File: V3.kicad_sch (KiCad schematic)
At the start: 30 parts, among them J1 USB_B, J2 Conn_01x02, J4 MAX9814, J5 OLED, J6 Heartbeat, Q1 AO3401A, U1 AP9101CK-CMTRG1, U2 AMS1117-3.3, U3 ESP32-S2-WROVER, U4 MMA8652FCR1

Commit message: Finalise schematic and start routing
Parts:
- removed TP2: TP_Battery+, TestPoint:TestPoint_Pad_D1.0mm, symbol Connector:TestPoint
- removed TP4: TP_Battery-, TestPoint:TestPoint_Pad_D1.0mm, symbol Connector:TestPoint
- removed U2: AMS1117-3.3, Package_TO_SOT_SMD:SOT-223-3_TabPin2, symbol Regulator_Linear:AMS1117-3.3
- added R8: 45K, Resistor_SMD:R_1206_3216Metric, symbol Device:R_Small
- added U2: XC6222B331MR-G, Package_TO_SOT_SMD:SOT-23-5, symbol Regulator_Linear:XC6220B331MR
- C1, C2: value 100uF -> 1uF; footprint Capacitor_SMD:C_1812_4532Metric -> Capacitor_SMD:C_1206_3216Metric
- J3: value (none) -> 47219-2001; footprint (none) -> 3rdparty:MOLEX_47219-2001
- Q3: value (none) -> BSD840NH6327XTSA1; footprint (none) -> Package_TO_SOT_SMD:SOT-363_SC-70-6
- renumbered TP5 to 3v3
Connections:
- net +3V3: now also R8.2, U2.5 (VOUT)
- net GND: now also U2.2 (GND)
- net VCC: now also U2.1 (VIN), U2.3 (CE)
- net at U3.21 (IO18): now also R8.1
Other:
- note added: "I2C Addr: 0x1D"
- note added: "Simulation: https://tinyurl.com/y7ddr9ho"
- moved on the sheet: 3v3, C2, C3, R5, TP6

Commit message: Finish routing and export gerbers
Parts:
- added R10, R9: 4.7K, Resistor_SMD:R_1206_3216Metric, symbol Device:R_Small
- added U5: USBLC6-2SC6, Package_TO_SOT_SMD:SOT-23-6, symbol Power_Protection:USBLC6-2SC6
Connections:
- net +3V3: now also R10.2, R9.2
- net GND: now also U5.2 (GND)
- net SCL: now also R10.1
- net SDA: now also R9.1
- net USB_D+: now also U5.1 (I/O1); no longer J1.3 (D+)
- net USB_D-: now also U5.3 (I/O2); no longer J1.2 (D-)
- net VBUS: now also U5.5 (VBUS)
- new net USB_CONN_D+: J1.3 (D+), U5.6 (I/O1)
- new net USB_CONN_D-: J1.2 (D-), U5.4 (I/O2)
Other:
- moved on the sheet: R4, R6, R7, U3

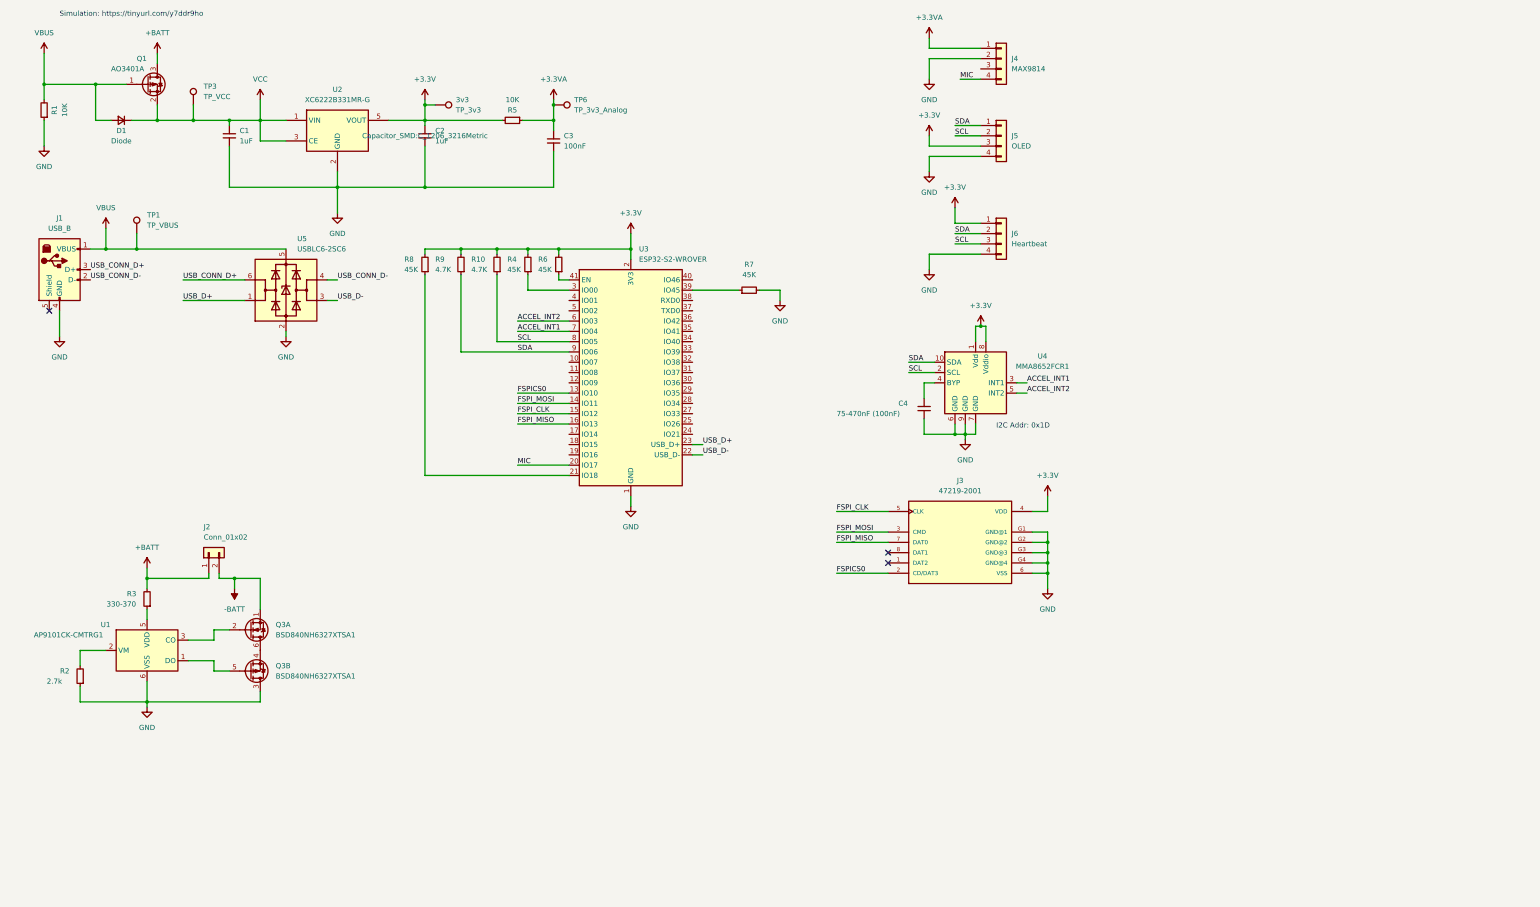
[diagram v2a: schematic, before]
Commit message: Add 3d models, pcb & schematic touch up, graphics, update gerbers and add step file
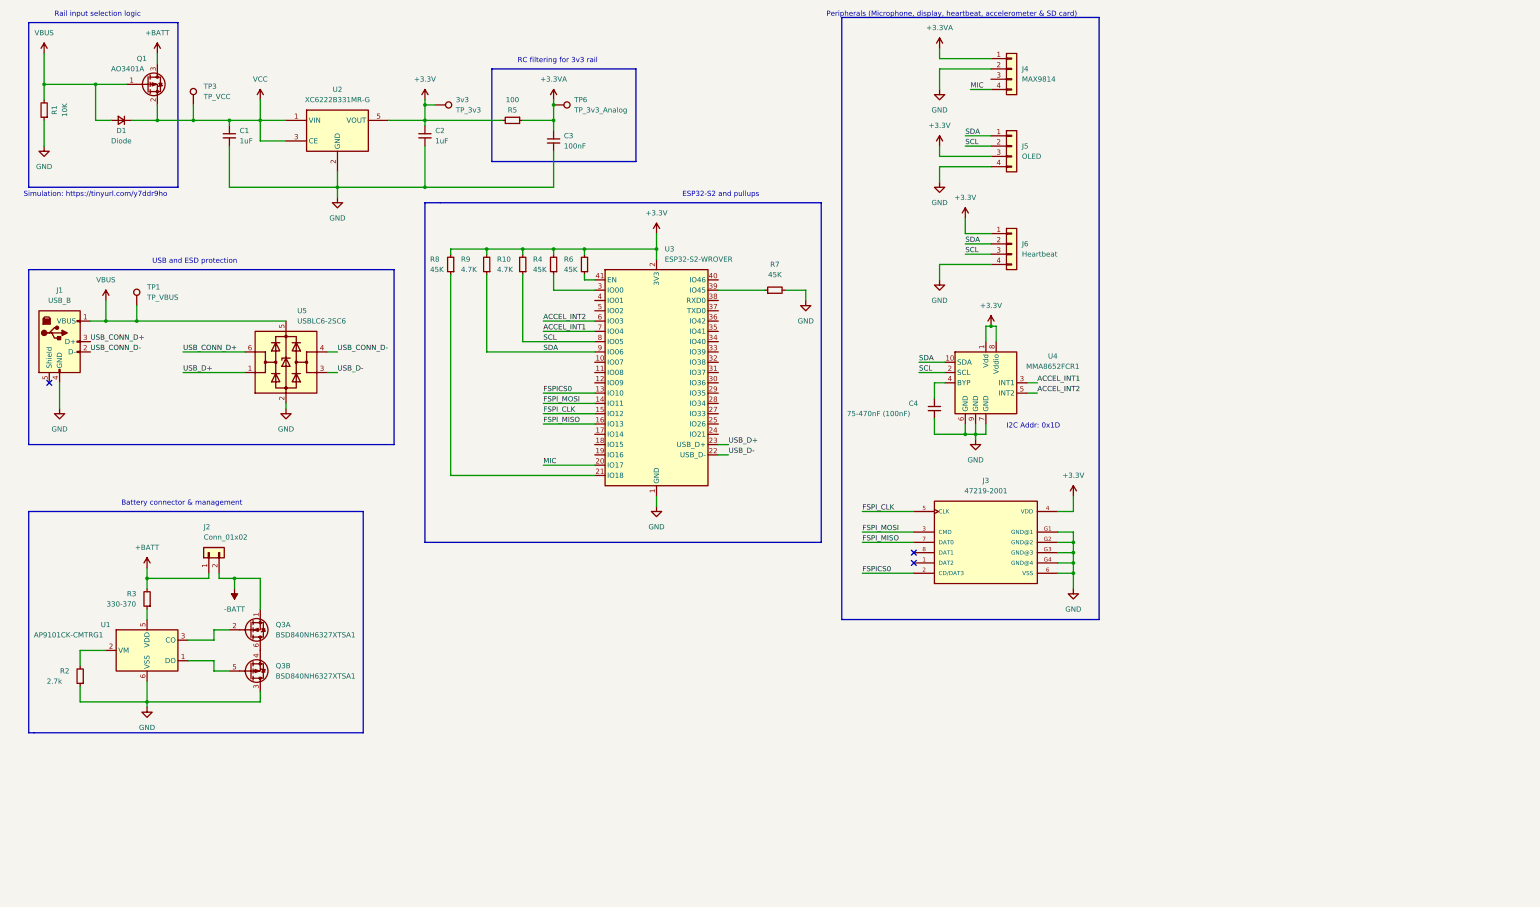
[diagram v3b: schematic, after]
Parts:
- R5: value 10K -> 100
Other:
- note added: "Battery connector & management"
- note added: "ESP32-S2 and pullups"
- note added: "Peripherals (Microphone, display, heartbeat, accelerometer & SD card)"
- note added: "RC filtering for 3v3 rail"
- note added: "Rail input selection logic"
- note added: "USB and ESD protection"
- moved on the sheet: C4, J1, J3, J4, J5, J6, R10, R4, R6, R7, R8, R9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

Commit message: Organisation
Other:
- note added: "1"
- note added: "10-4-2022"
- note added: "2.0"
- note added: "Project Integration PCB team PintApple"
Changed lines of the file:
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@@
+    (effects (font (size 1.27 1.27)) (justify left bottom))
+  )
+  (text "1" (at 187.96 184.15 0)
     (effects (font (size 1.27 1.27)) (justify left bottom))
   )
   (text "Battery connector & management" (at 40.64 135.89 0)
+    (effects (font (size 1.27 1.27)) (justify left bottom))
+  )
+  (text "10-4-2022" (at 206.6363 194.1101 0)
     (effects (font (size 1.27 1.27)) (justify left bottom))
   )
@@
   )
   (text "ESP32-S2 and pullups" (at 179.07 59.69 0)
+    (effects (font (size 1.27 1.27)) (justify left bottom))
+  )
+  (text "Project Integration PCB team PintApple" (at 186.69 190.5 0)
     (effects (font (size 1.27 1.27)) (justify left bottom))
   )
@@
     (effects (font (size 1.27 1.27)) (justify left bottom))
   )
+  (text "2.0" (at 268.267 194.2398 0)
+    (effects (font (size 1.27 1.27)) (justify left bottom))
+  )

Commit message: Switch out micro USB for USB-C
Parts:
- removed 3v3: TP_3v3, TestPoint:TestPoint_Pad_D1.0mm, symbol Connector:TestPoint
- removed J1: USB_B, Connector_USB:USB_Micro-B_Wuerth_629105150521, symbol Connector:USB_B
- added J1: USB_C_Plug_USB2.0, Connector_USB:USB_C_Receptacle_GCT_USB4085, symbol Connector:USB_C_Plug_USB2.0
- added R11, R12: 4.7K, Resistor_SMD:R_1206_3216Metric, symbol Device:R_Small
- added R13, R14: 100, Resistor_SMD:R_1206_3216Metric, symbol Device:R_Small
- TP3: renamed from TP6; value TP_3v3_Analog -> TP_3.3VA
- renumbered TP3 to TP2
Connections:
- net +3.3VA: no longer TP3.1
- net +3V3: now also TP3.1
- net GND: now also J1.A1 (GND), J1.A12 (GND), J1.B1 (GND), J1.B12 (GND), J1.S1 (SHIELD), R11.1, R12.1
- net USB_CONN_D+: now also U5.4 (I/O2), J1.A6 (D+); no longer U5.6 (I/O1)
- net USB_CONN_D-: now also U5.6 (I/O1), J1.A7 (D-); no longer U5.4 (I/O2)
- net USB_D+: now also R14.1; no longer U5.1 (I/O1)
- net USB_D-: now also R13.1; no longer U5.3 (I/O2)
- net VBUS: now also J1.A4 (VBUS), J1.A9 (VBUS), J1.B4 (VBUS), J1.B9 (VBUS)
- new net: J1.A5 (CC), R12.2
- new net: R13.2, U5.1 (I/O1)
- new net: J1.B5 (VCONN), R11.2
- new net: R14.2, U5.3 (I/O2)
- no-connect marks 3 -> 2
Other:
- moved on the sheet: C3, J2, Q3A, Q3B, R2, R3, R5, TP1, TP3, U1, U5

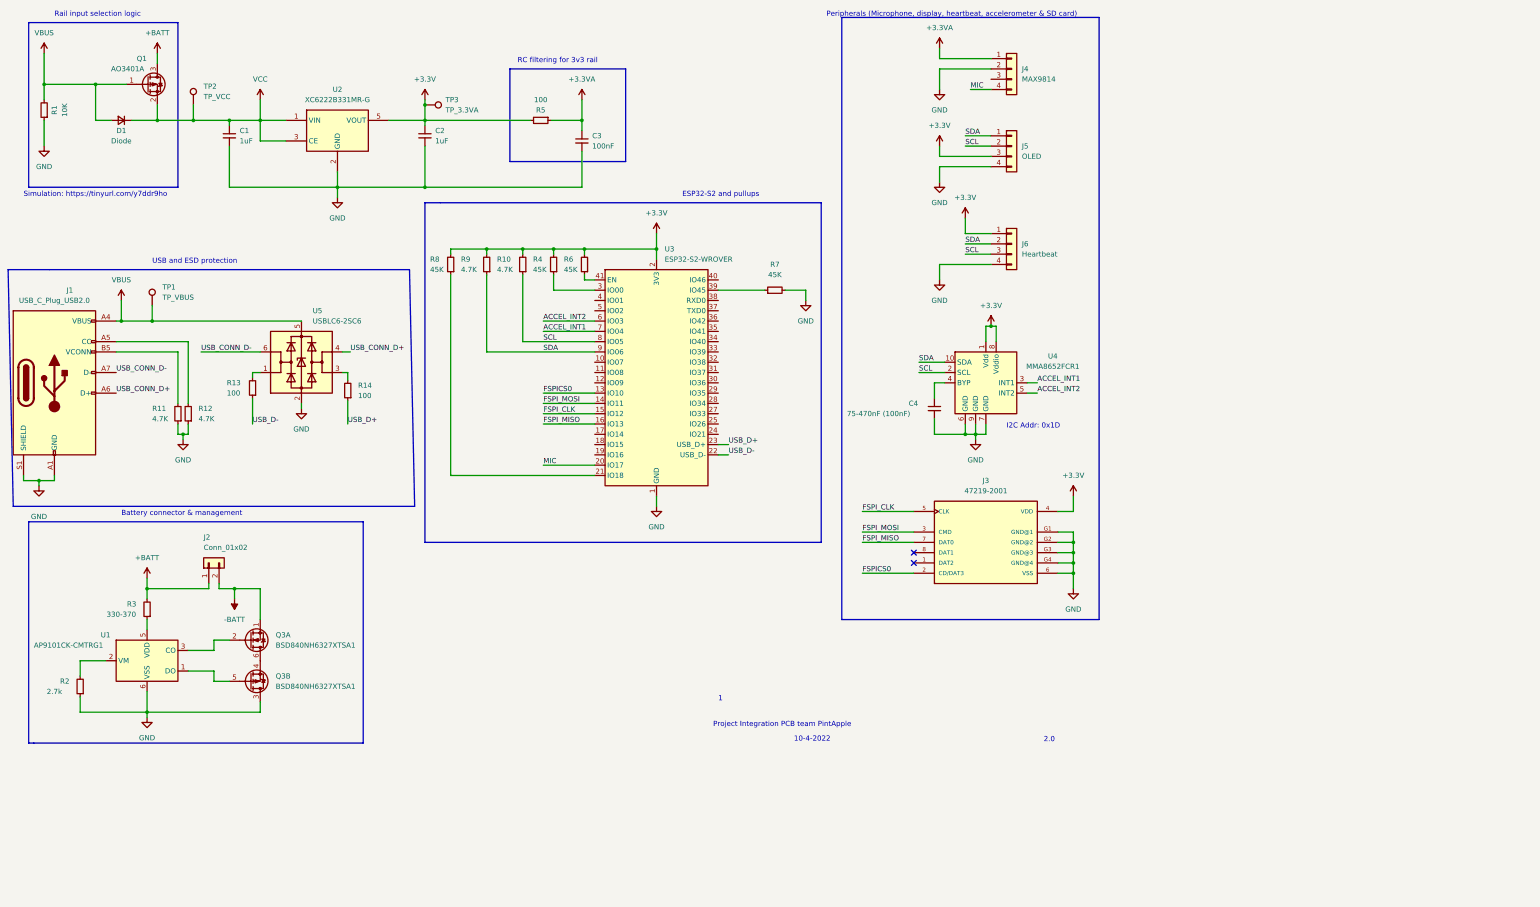
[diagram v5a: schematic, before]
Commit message: Add USB-C port
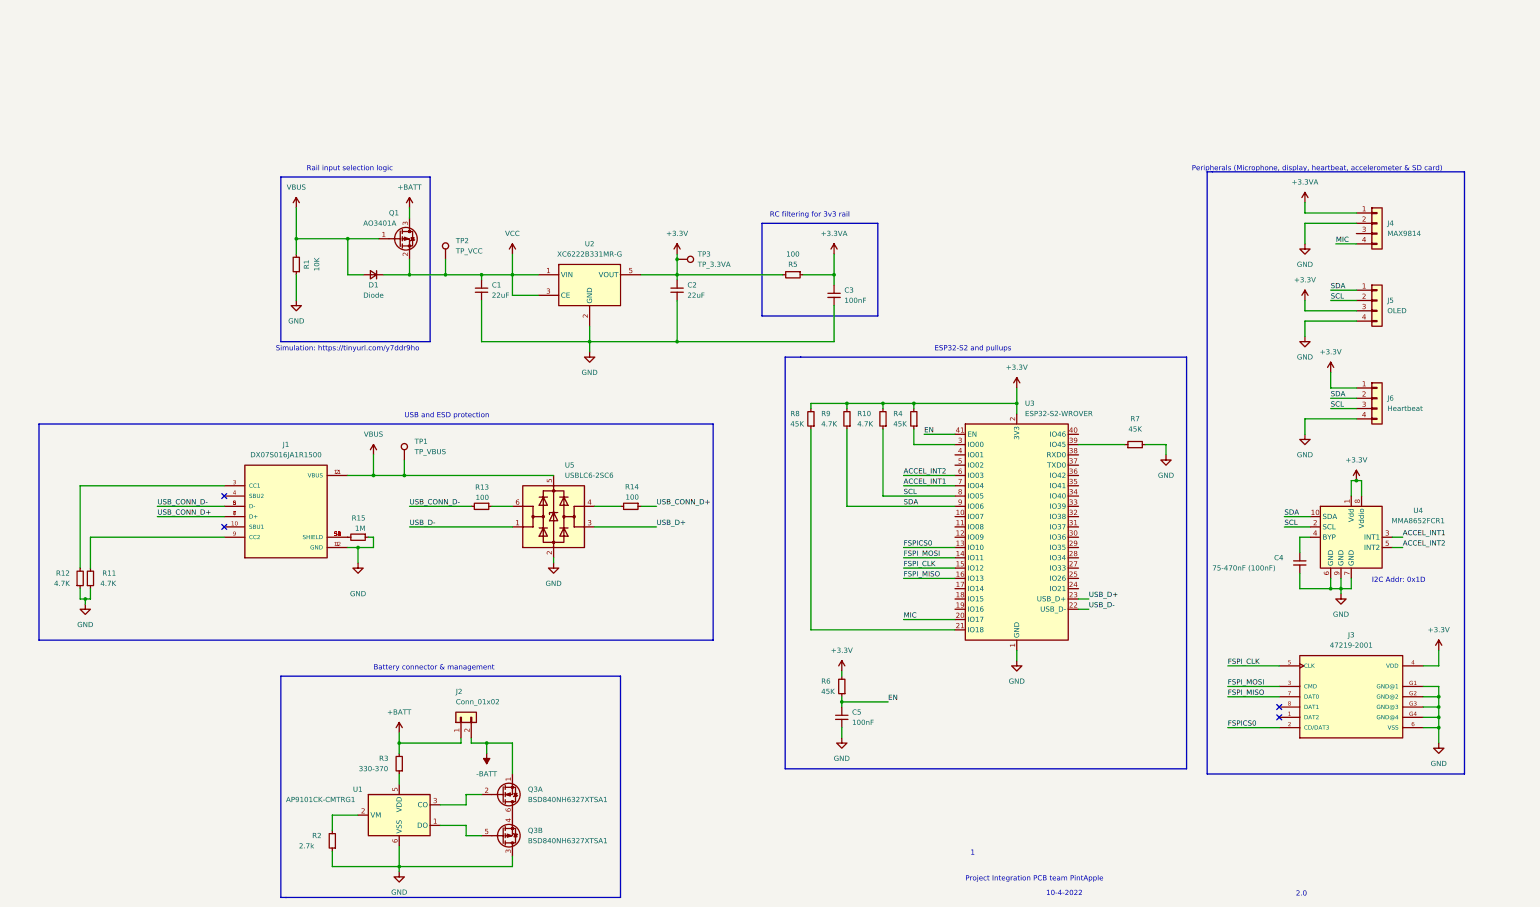
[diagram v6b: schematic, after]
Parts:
- removed J1: USB_C_Plug_USB2.0, Connector_USB:USB_C_Receptacle_GCT_USB4085, symbol Connector:USB_C_Plug_USB2.0
- added C5: 100nF, Capacitor_SMD:C_1206_3216Metric, symbol Device:C_Small
- added J1: DX07S016JA1R1500, JAE_DX07S016JA1R1500, symbol USB-C:DX07S016JA1R1500
- added R15: 1M, Resistor_SMD:R_1206_3216Metric, symbol Device:R_Small
- C1, C2: value 1uF -> 22uF
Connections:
- net GND: now also C5.2, J1.1 (GND), J1.12 (GND), R15.1
- net USB_CONN_D+: now also R14.1, J1.6 (D+), J1.7 (D+); no longer U5.4 (I/O2)
- net USB_CONN_D-: now also R13.2, J1.5 (D-), J1.8 (D-); no longer U5.6 (I/O1)
- net USB_D+: now also U5.3 (I/O2); no longer R14.1
- net USB_D-: now also U5.1 (I/O1); no longer R13.1
- net VBUS: now also J1.11 (VBUS), J1.2 (VBUS)
- net EN: now reaches R6.1, U3.41 (EN)
- net EN: now also C5.1
- net at R12.2: now also J1.3 (CC1)
- net at R11.2: now also J1.9 (CC2)
- net at R14.2: now also U5.4 (I/O2); no longer U5.3 (I/O2)
- new net: R13.1, U5.6 (I/O1)
- new net: J1.S1 (SHIELD), J1.S2 (SHIELD), J1.S3 (SHIELD), J1.S4 (SHIELD), J1.S5 (SHIELD), J1.S6 (SHIELD), R15.2
- no-connect marks 2 -> 4
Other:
- moved on the sheet: C1, C2, C3, C4, D1, J2, J3, J4, J5, J6, Q1, Q3A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
